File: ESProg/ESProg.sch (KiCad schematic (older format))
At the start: 4 parts, among them J1 6_PIN_SERIAL_CABLEPTH, U1 ESP8266-ESP-01

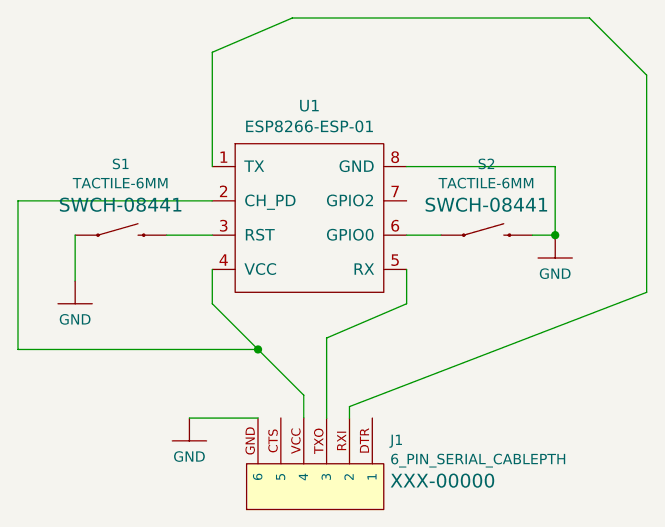
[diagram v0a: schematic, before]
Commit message: Update with Hackster logo
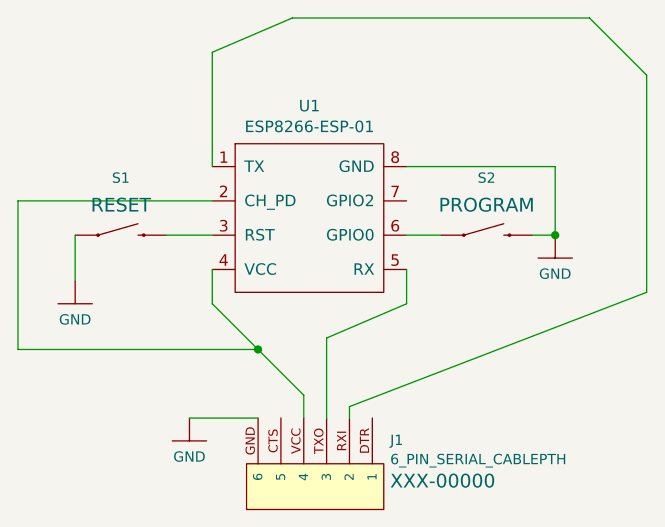
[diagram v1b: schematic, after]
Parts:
- S1: Field4 SWCH-08441 -> RESET
- S2: value TACTILE-6MM -> BUTTON; Field4 SWCH-08441 -> PROGRAM
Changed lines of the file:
@@
 U 1 1 60137075
 P 4950 3250
-F 0 "S1" H 4950 3560 45  0000 C CNN
-F 1 "TACTILE-6MM" H 4950 3476 45  0000 C CNN
+F 0 "S1" H 4950 3500 45  0000 C CNN
+F 1 "TACTILE-6MM" H 4950 3476 45  0001 C CNN
 F 2 "Switches:TACTILE_SWITCH_PTH_6.0MM" H 4950 3450 20  0001 C CNN
 F 3 "" H 4950 3250 50  0001 C CNN
-F 4 " SWCH-08441" H 4950 3381 60  0000 C CNN "Field4"
+F 4 "RESET" H 4950 3381 60  0000 C CNN "Field4"
 	1    4950 3250
 	1    0    0    -1
@@
 U 1 1 6013DBAB
 P 6550 3250
-F 0 "S2" H 6550 3560 45  0000 C CNN
-F 1 "TACTILE-6MM" H 6550 3476 45  0000 C CNN
+F 0 "S2" H 6550 3500 45  0000 C CNN
+F 1 "BUTTON" H 6550 3476 45  0001 C CNN
 F 2 "Switches:TACTILE_SWITCH_PTH_6.0MM" H 6550 3450 20  0001 C CNN
 F 3 "" H 6550 3250 50  0001 C CNN
-F 4 " SWCH-08441" H 6550 3381 60  0000 C CNN "Field4"
+F 4 "PROGRAM" H 6550 3381 60  0000 C CNN "Field4"
 	1    6550 3250
 	1    0    0    -1
